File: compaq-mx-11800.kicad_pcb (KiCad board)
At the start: 2 copper layers, 246 parts

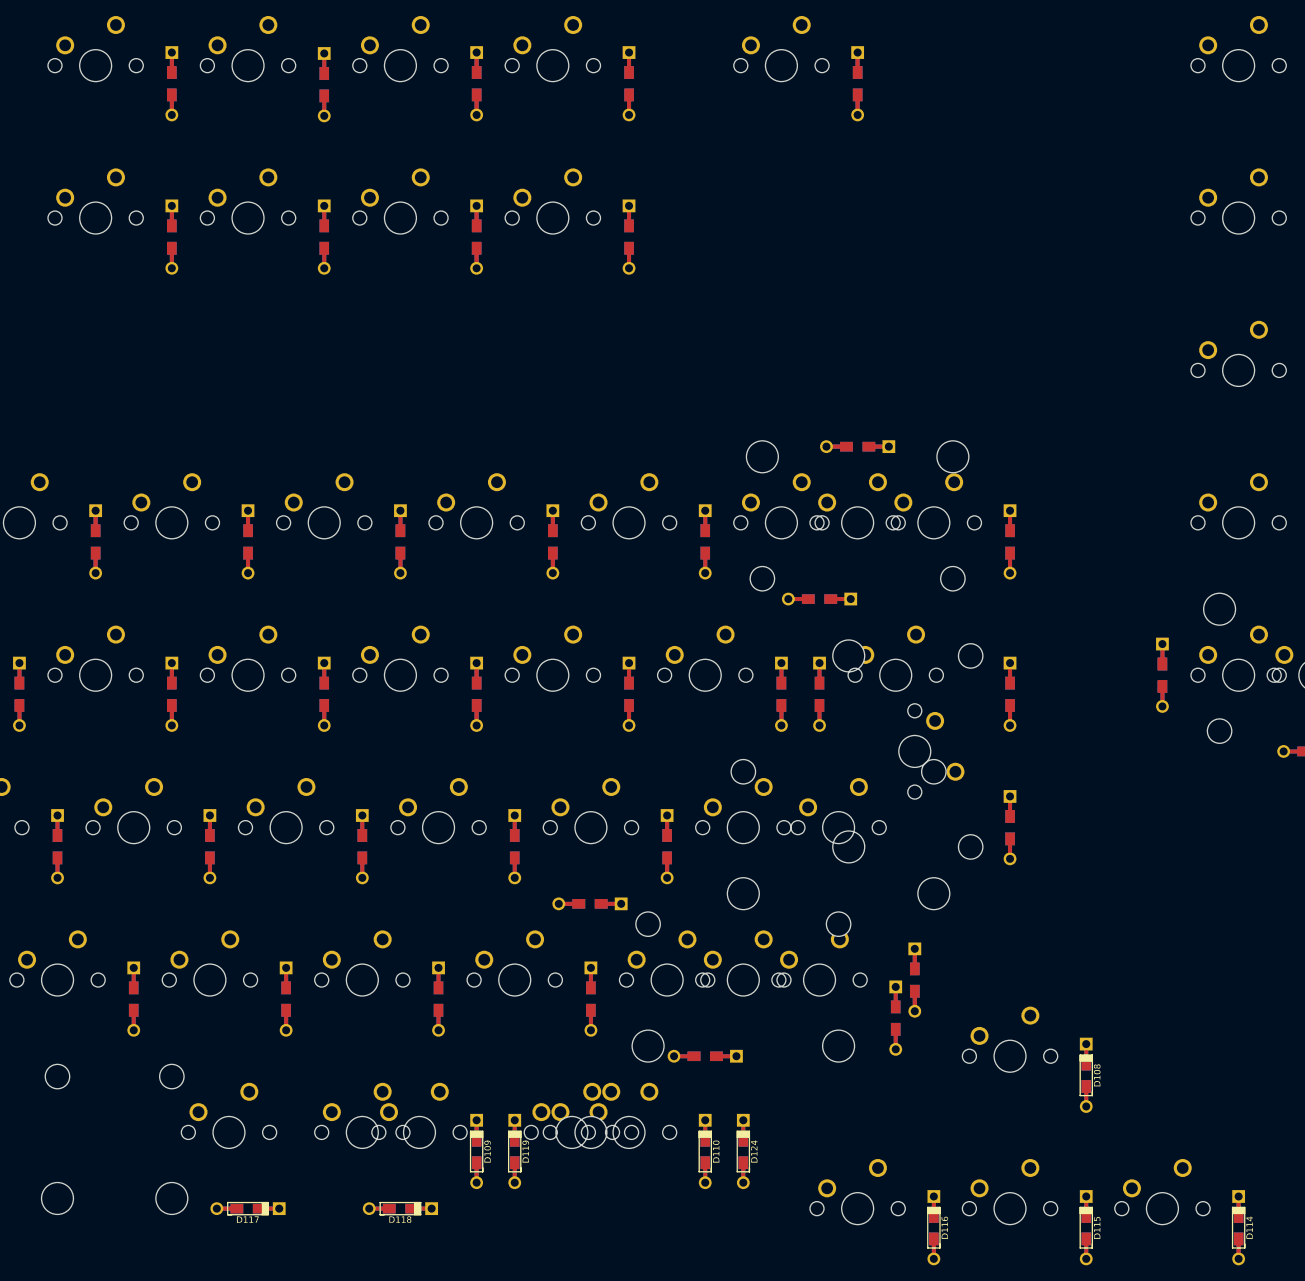
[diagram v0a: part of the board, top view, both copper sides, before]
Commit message: correct row and column placement on pcb
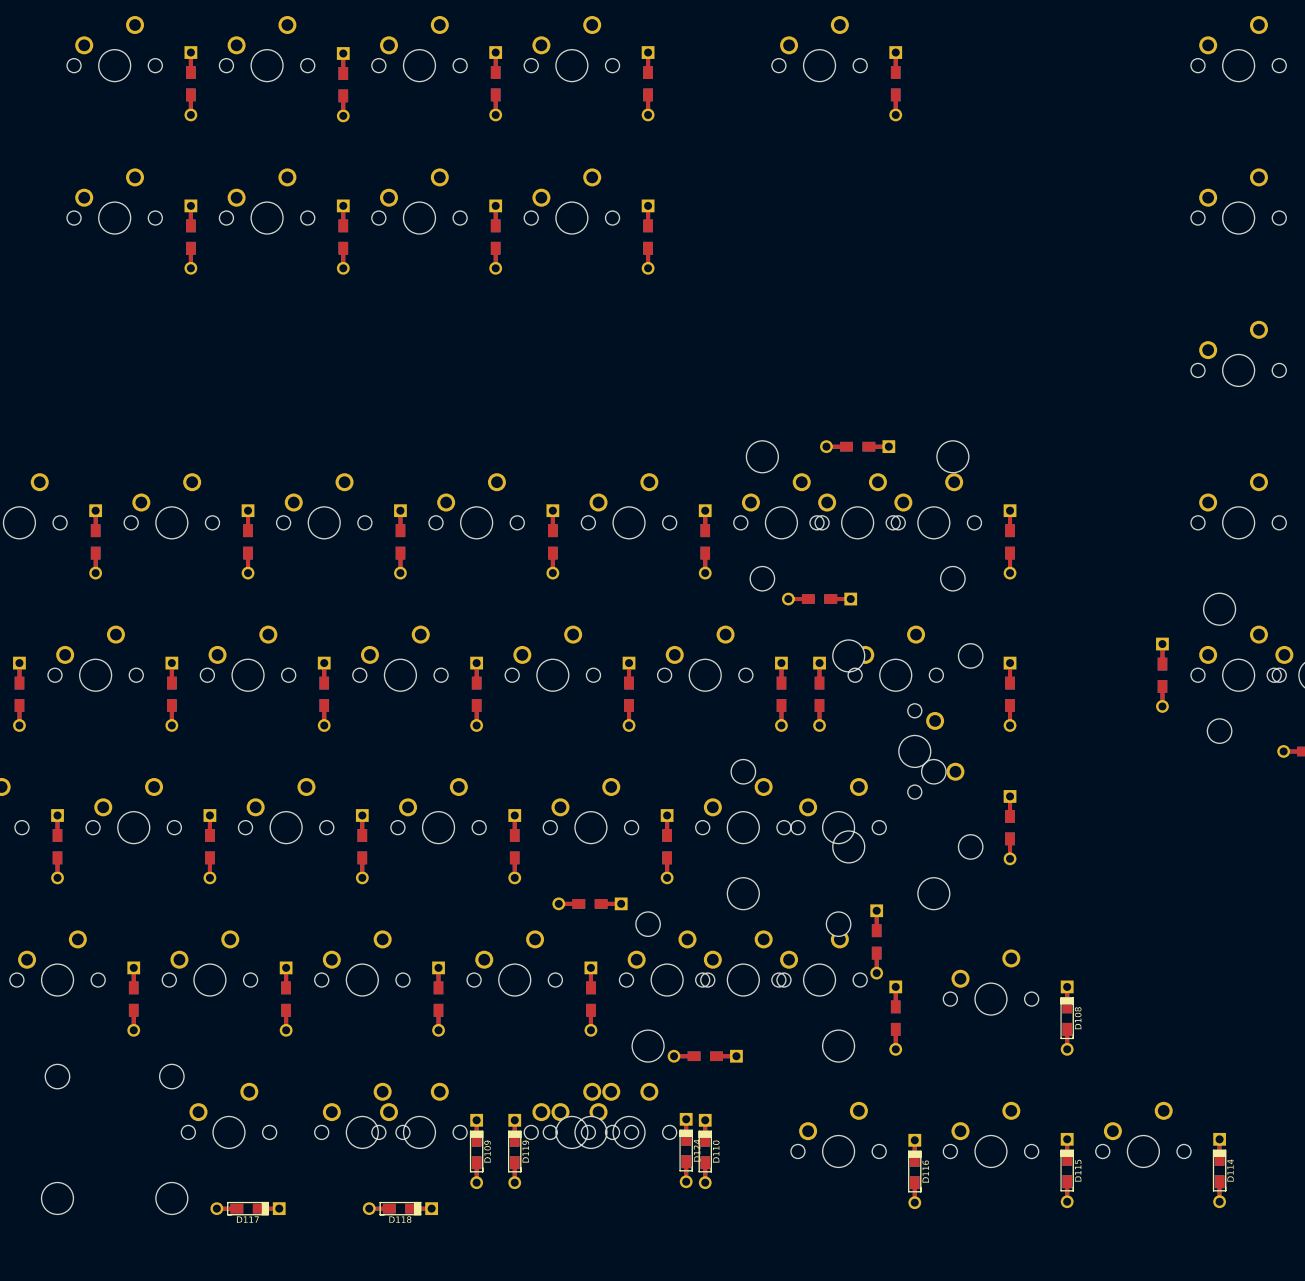
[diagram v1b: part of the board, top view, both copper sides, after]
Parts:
- moved MX114 7.53 mm to (259.6, 195.3)
- moved D108 7.53 mm to (250.0, 178.6)
- moved MX115 7.53 mm to (240.5, 195.3)
- moved MX116 7.53 mm to (221.5, 195.3)
- moved D115 7.53 mm to (250.0, 197.6)
- moved MX108 7.53 mm to (240.5, 176.2)
- moved D114 7.53 mm to (269.1, 197.6)
- moved D116 7.42 mm to (231.0, 197.8)
- moved D124 7.14 mm to (202.4, 195.1)
- moved D107 6.74 mm to (226.2, 169.1)
- moved D12 4.76 mm to (228.6, 61.8)
- moved MX12 4.76 mm to (219.1, 59.5)
- moved D11 2.38 mm to (197.6, 61.8)
- moved D27 2.38 mm to (197.6, 81.0)
- moved MX25 2.38 mm to (150.0, 78.6)
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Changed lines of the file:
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@@
   )
   (module Keebio-Parts:Diode-dual (layer F.Cu)
-    (at 209.55 195.2625 90)
+    (at 202.40625 195.14375 90)
     (attr smd)
     (fp_text reference D124 (at -0.0254 1.4 90) (layer F.SilkS)
@@
   )
   (module MX_Only:MXOnly-1U-NoLED (layer F.Cu)
-    (at 223.8375 202.40625)
+    (at 221.45625 195.2625)
     (fp_text reference MX116 (at 0 3.175) (layer Dwgs.User)
       (effects (font (size 1 1) (thickness 0.15)))
@@
   )
   (module MX_Only:MXOnly-1U-NoLED (layer F.Cu)
-    (at 242.8875 202.40625)
+    (at 240.50625 195.2625)
     (fp_text reference MX115 (at 0 3.175) (layer Dwgs.User)
       (effects (font (size 1 1) (thickness 0.15)))
@@
   )
   (module MX_Only:MXOnly-1U-NoLED (layer F.Cu)
-    (at 261.9375 202.40625)
+    (at 259.55625 195.2625)
     (fp_text reference MX114 (at 0 3.175) (layer Dwgs.User)
       (effects (font (size 1 1) (thickness 0.15)))
@@
   )
   (module MX_Only:MXOnly-1U-NoLED (layer F.Cu)
-    (at 242.8875 183.35625)
+    (at 240.50625 176.2125)
     (fp_text reference MX108 (at 0 3.175) (layer Dwgs.User)
       (effects (font (size 1 1) (thickness 0.15)))
@@
   )
   (module Keebio-Parts:Diode-dual (layer F.Cu)
-    (at 233.3625 204.7875 90)
+    (at 230.98125 197.7625 90)
     (attr smd)
     (fp_text reference D116 (at -0.0254 1.4 90) (layer F.SilkS)
@@
   )
   (module Keebio-Parts:Diode-dual (layer F.Cu)
-    (at 252.4125 204.7875 90)
+    (at 250.03125 197.64375 90)
     (attr smd)
     (fp_text reference D115 (at -0.0254 1.4 90) (layer F.SilkS)
@@
   )
   (module Keebio-Parts:Diode-dual (layer F.Cu)
-    (at 271.4625 204.7875 90)
+    (at 269.08125 197.64375 90)
     (attr smd)
     (fp_text reference D114 (at -0.0254 1.4 90) (layer F.SilkS)
@@
   )
   (module Keebio-Parts:Diode-dual (layer F.Cu)
-    (at 252.4125 185.7375 90)
+    (at 250.03125 178.59375 90)
     (attr smd)
     (fp_text reference D108 (at -0.0254 1.4 90) (layer F.SilkS)
@@
   )
   (module Keebio-Parts:Diode-dual (layer B.Cu)
-    (at 230.98125 173.83125 90)
+    (at 226.21875 169.06875 90)
     (attr smd)
     (fp_text reference D107 (at -0.0254 -1.4 90) (layer B.SilkS)
@@
   )
   (module MX_Only:MXOnly-1U-NoLED (layer F.Cu)
-    (at 185.7375 78.58125)
+    (at 188.11875 78.58125)
     (fp_text reference MX27 (at 0 3.175) (layer Dwgs.User)
       (effects (font (size 1 1) (thickness 0.15)))
@@
   )
   (module MX_Only:MXOnly-1U-NoLED (layer F.Cu)
-    (at 166.6875 78.58125)
+    (at 169.06875 78.58125)
     (fp_text reference MX26 (at 0 3.175) (layer Dwgs.User)
       (effects (font (size 1 1) (thickness 0.15)))
@@
   )
   (module MX_Only:MXOnly-1U-NoLED (layer F.Cu)
-    (at 147.6375 78.58125)
+    (at 150.01875 78.58125)
     (fp_text reference MX25 (at 0 3.175) (layer Dwgs.User)
       (effects (font (size 1 1) (thickness 0.15)))
@@
   )
   (module MX_Only:MXOnly-1U-NoLED (layer F.Cu)
-    (at 128.5875 78.58125)
+    (at 130.96875 78.58125)
     (fp_text reference MX24 (at 0 3.175) (layer Dwgs.User)
       (effects (font (size 1 1) (thickness 0.15)))
@@
   )
   (module MX_Only:MXOnly-1U-NoLED (layer F.Cu)
-    (at 214.3125 59.53125)
+    (at 219.075 59.53125)
     (fp_text reference MX12 (at 0 3.175) (layer Dwgs.User)
       (effects (font (size 1 1) (thickness 0.15)))
@@
   )
   (module MX_Only:MXOnly-1U-NoLED (layer F.Cu)
-    (at 185.7375 59.53125)
+    (at 188.11875 59.53125)
     (fp_text reference MX11 (at 0 3.175) (layer Dwgs.User)
       (effects (font (size 1 1) (thickness 0.15)))
@@
   )
   (module MX_Only:MXOnly-1U-NoLED (layer F.Cu)
-    (at 166.6875 59.53125)
+    (at 169.06875 59.53125)
     (fp_text reference MX10 (at 0 3.175) (layer Dwgs.User)
       (effects (font (size 1 1) (thickness 0.15)))
@@
   )
   (module MX_Only:MXOnly-1U-NoLED (layer F.Cu)
-    (at 147.6375 59.53125)
+    (at 150.01875 59.53125)
     (fp_text reference MX9 (at 0 3.175) (layer Dwgs.User)
       (effects (font (size 1 1) (thickness 0.15)))
@@
   )
   (module MX_Only:MXOnly-1U-NoLED (layer F.Cu)
-    (at 128.5875 59.53125)
+    (at 130.96875 59.53125)
     (fp_text reference MX8 (at 0 3.175) (layer Dwgs.User)
       (effects (font (size 1 1) (thickness 0.15)))
@@
   )
   (module Keebio-Parts:Diode-dual (layer B.Cu)
-    (at 195.2625 80.9625 90)
+    (at 197.64375 80.9625 90)
     (attr smd)
     (fp_text reference D27 (at -0.0254 -1.4 90) (layer B.SilkS)
@@
   )
   (module Keebio-Parts:Diode-dual (layer B.Cu)
-    (at 176.2125 80.9625 90)
+    (at 178.59375 80.9625 90)
     (attr smd)
     (fp_text reference D26 (at -0.0254 -1.4 90) (layer B.SilkS)
@@
   )
   (module Keebio-Parts:Diode-dual (layer B.Cu)
-    (at 157.1625 80.9625 90)
+    (at 159.54375 80.9625 90)
     (attr smd)
     (fp_text reference D25 (at -0.0254 -1.4 90) (layer B.SilkS)
@@
   )
   (module Keebio-Parts:Diode-dual (layer B.Cu)
-    (at 138.1125 80.9625 90)
+    (at 140.49375 80.9625 90)
     (attr smd)
     (fp_text reference D24 (at -0.0254 -1.4 90) (layer B.SilkS)
@@
   )
   (module Keebio-Parts:Diode-dual (layer B.Cu)
-    (at 223.8375 61.79375 90)
+    (at 228.6 61.79375 90)
     (attr smd)
     (fp_text reference D12 (at -0.0254 -1.4 90) (layer B.SilkS)
@@
   )
   (module Keebio-Parts:Diode-dual (layer B.Cu)
-    (at 195.2625 61.79375 90)
+    (at 197.64375 61.79375 90)
     (attr smd)
     (fp_text reference D11 (at -0.0254 -1.4 90) (layer B.SilkS)
@@
   )
   (module Keebio-Parts:Diode-dual (layer B.Cu)
-    (at 176.2125 61.79375 90)
+    (at 178.59375 61.79375 90)
     (attr smd)
     (fp_text reference D10 (at -0.0254 -1.4 90) (layer B.SilkS)
@@
   )
   (module Keebio-Parts:Diode-dual (layer B.Cu)
-    (at 157.1625 61.9125 90)
+    (at 159.54375 61.9125 90)
     (attr smd)
     (fp_text reference D9 (at -0.0254 -1.4 90) (layer B.SilkS)
@@
   )
   (module Keebio-Parts:Diode-dual (layer B.Cu)
-    (at 138.1125 61.79375 90)
+    (at 140.49375 61.79375 90)
     (attr smd)
     (fp_text reference D8 (at -0.0254 -1.4 90) (layer B.SilkS)

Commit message: draw board outline
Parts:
- moved MX114 4.76 mm to (264.3, 195.3)
- moved MX108 4.76 mm to (245.3, 176.2)
- moved MX115 4.76 mm to (245.3, 195.3)
- moved MX116 4.76 mm to (226.2, 195.3)
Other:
- board outline added: 387.1 x 166.4 mm

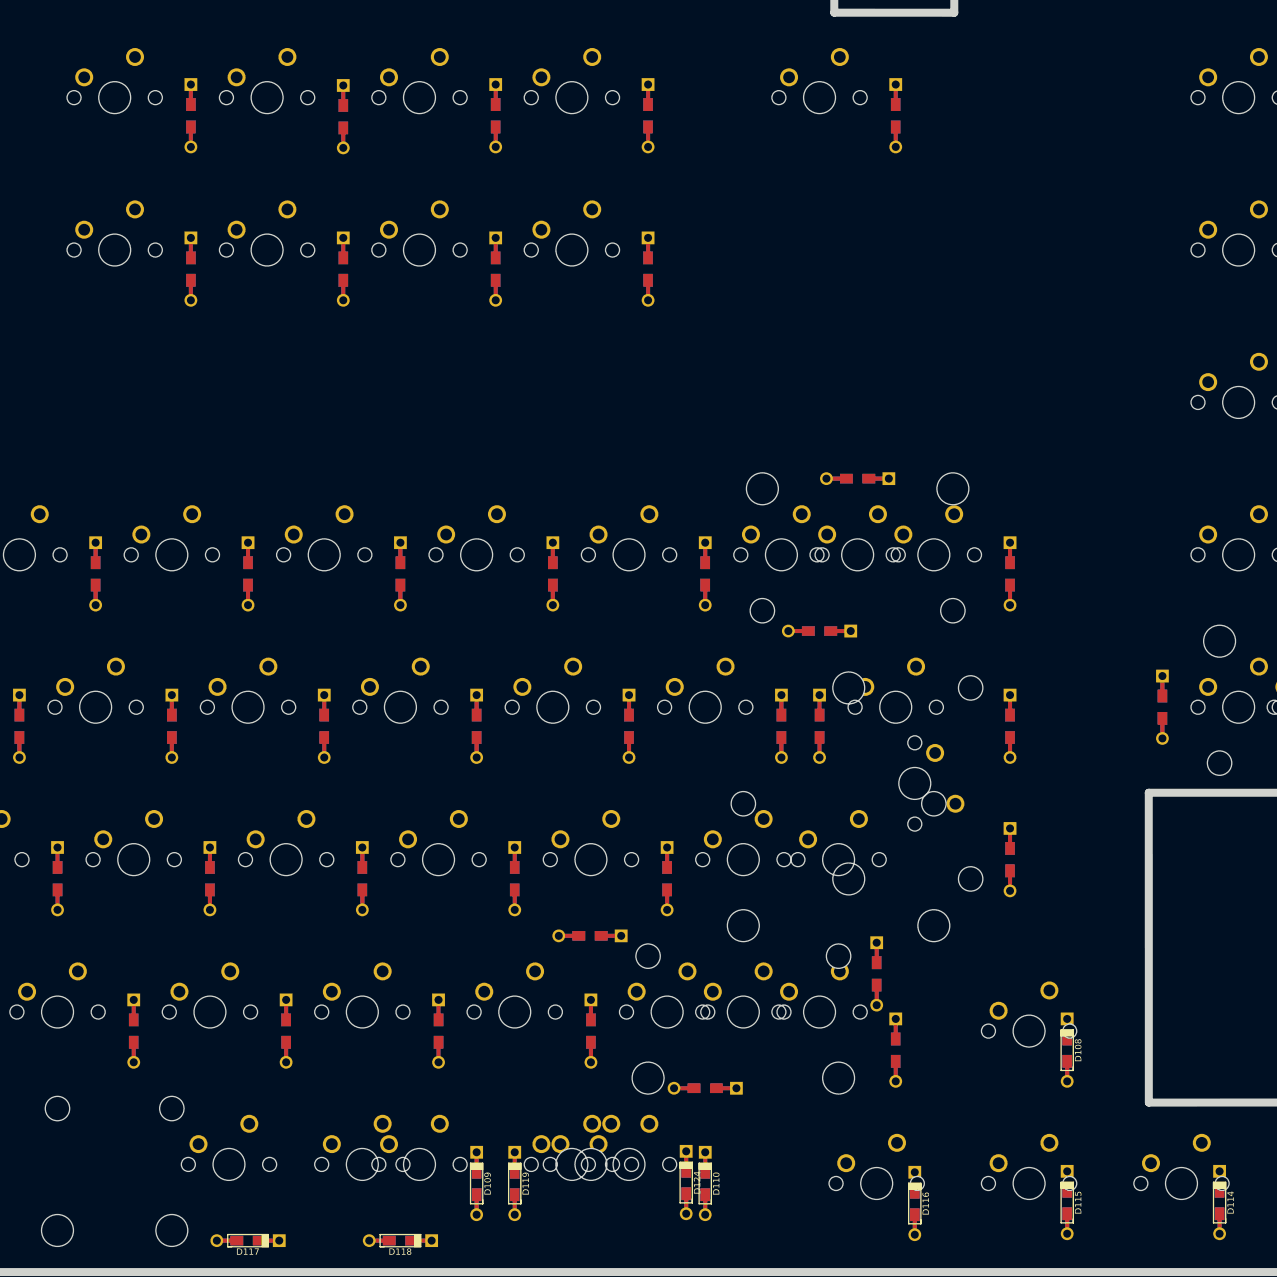
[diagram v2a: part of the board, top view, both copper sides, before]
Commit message: adjust arrow cluster spacing
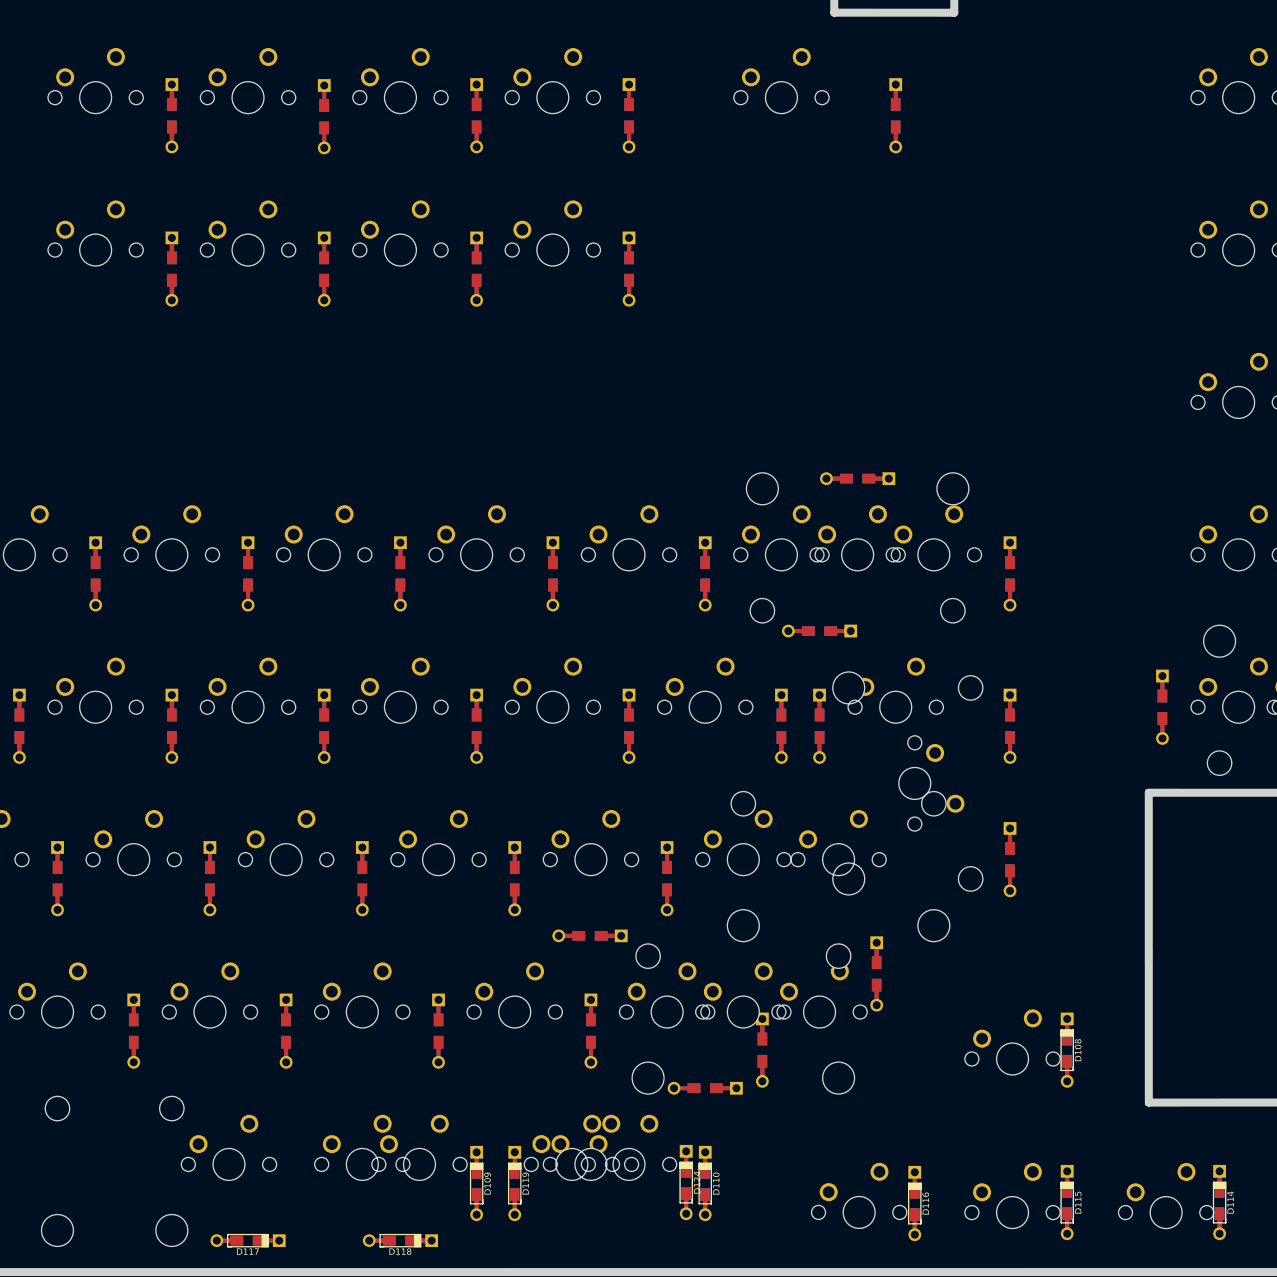
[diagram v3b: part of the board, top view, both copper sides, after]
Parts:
- moved D92 16.7 mm to (211.9, 178.6)
- moved MX12 4.76 mm to (214.3, 59.5)
- moved MX116 4.23 mm to (224.0, 198.9)
- moved MX115 4.18 mm to (243.2, 198.9)
- moved MX114 4.11 mm to (262.4, 198.9)
- moved MX108 4.05 mm to (243.2, 179.7)
- moved D11 2.38 mm to (195.3, 61.8)
- moved D27 2.38 mm to (195.3, 81.0)
- moved MX25 2.38 mm to (147.6, 78.6)
- moved MX9 2.38 mm to (147.6, 59.5)
- moved D10 2.38 mm to (176.2, 61.8)
- moved D24 2.38 mm to (138.1, 81.0)
- moved D25 2.38 mm to (157.2, 81.0)
- moved D26 2.38 mm to (176.2, 81.0)
- moved D8 2.38 mm to (138.1, 61.8)
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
